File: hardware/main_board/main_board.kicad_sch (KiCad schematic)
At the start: 4 parts

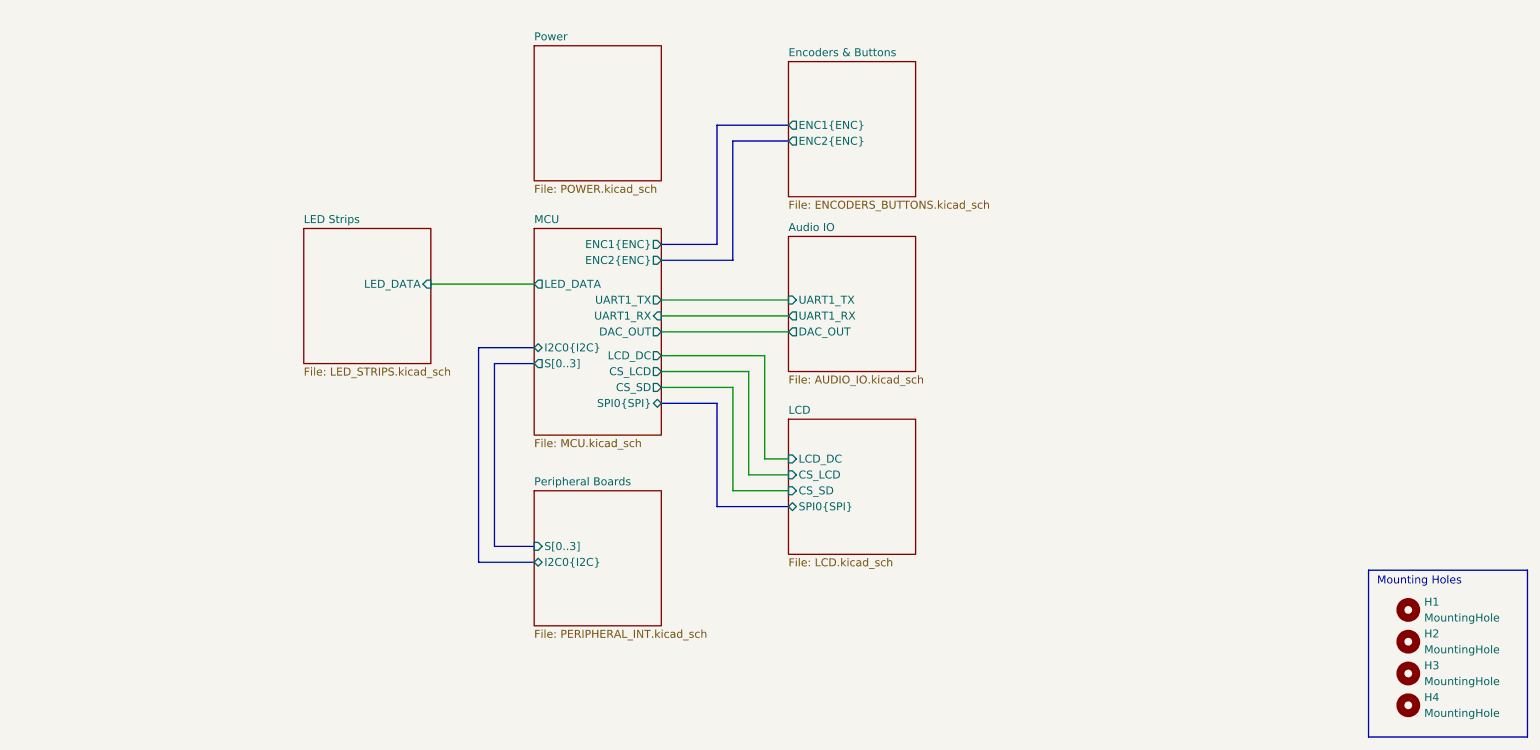
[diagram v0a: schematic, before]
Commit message: main board stuff. removed usbc for power. added level shifter for led logic signal. added lights for mux select signals. finished layout + pass DRC
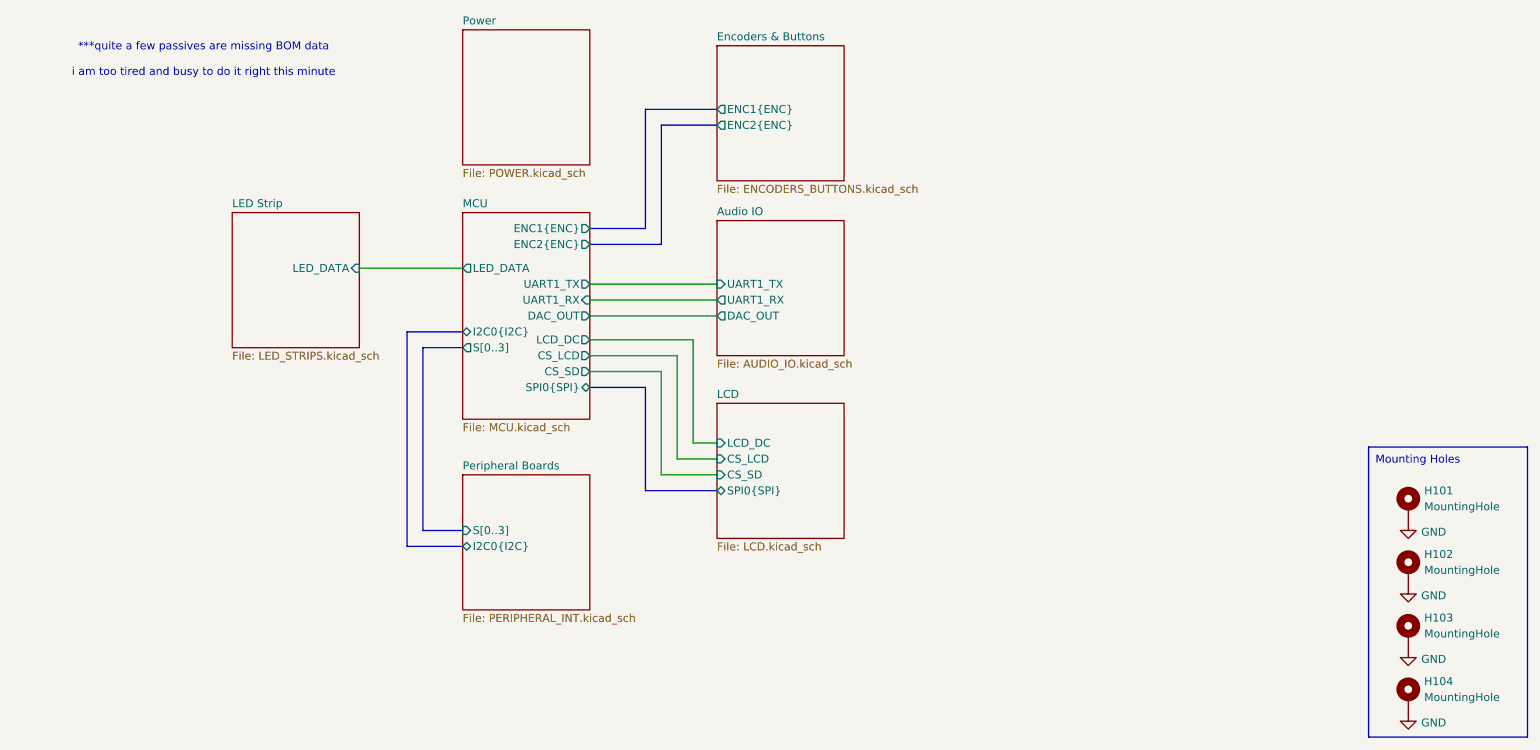
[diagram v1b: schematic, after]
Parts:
- H101: renamed from H1; footprint MountingHole:MountingHole_3.2mm_M3 -> SamacSys_Parts:standoff_MH; symbol Mechanical:MountingHole -> Mechanical:MountingHole_Pad
- H102: renamed from H2; footprint MountingHole:MountingHole_3.2mm_M3 -> SamacSys_Parts:standoff_MH; symbol Mechanical:MountingHole -> Mechanical:MountingHole_Pad
- H103: renamed from H3; footprint MountingHole:MountingHole_3.2mm_M3 -> SamacSys_Parts:standoff_MH; symbol Mechanical:MountingHole -> Mechanical:MountingHole_Pad
- H104: renamed from H4; footprint MountingHole:MountingHole_3.2mm_M3 -> SamacSys_Parts:standoff_MH; symbol Mechanical:MountingHole -> Mechanical:MountingHole_Pad
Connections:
- new net GND: H101.1, H102.1, H103.1, H104.1
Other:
- sheet LED Strips renamed LED Strip
- note added: "***quite a few passives are missing BOM data i am too tired and busy to do it right this minute"
- company: (none) -> Lakshay Lovers
- title: (none) -> Imagiano Main Board

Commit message: bom
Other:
- note removed: "***quite a few passives are missing BOM data i am too tired and busy to do it right this minute"
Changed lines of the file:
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@@
-		)
-	)
-	(text "***quite a few passives are missing BOM data\n\ni am too tired and busy to do it right this minute"
-		(exclude_from_sim no)
-		(at 69.088 53.086 0)
-		(effects
-			(font
-				(size 1.27 1.27)
-			)
 		)
 	)
